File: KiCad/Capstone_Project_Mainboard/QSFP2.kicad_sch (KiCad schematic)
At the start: 12 parts, among them J4 QSFP+ Connector & Cage

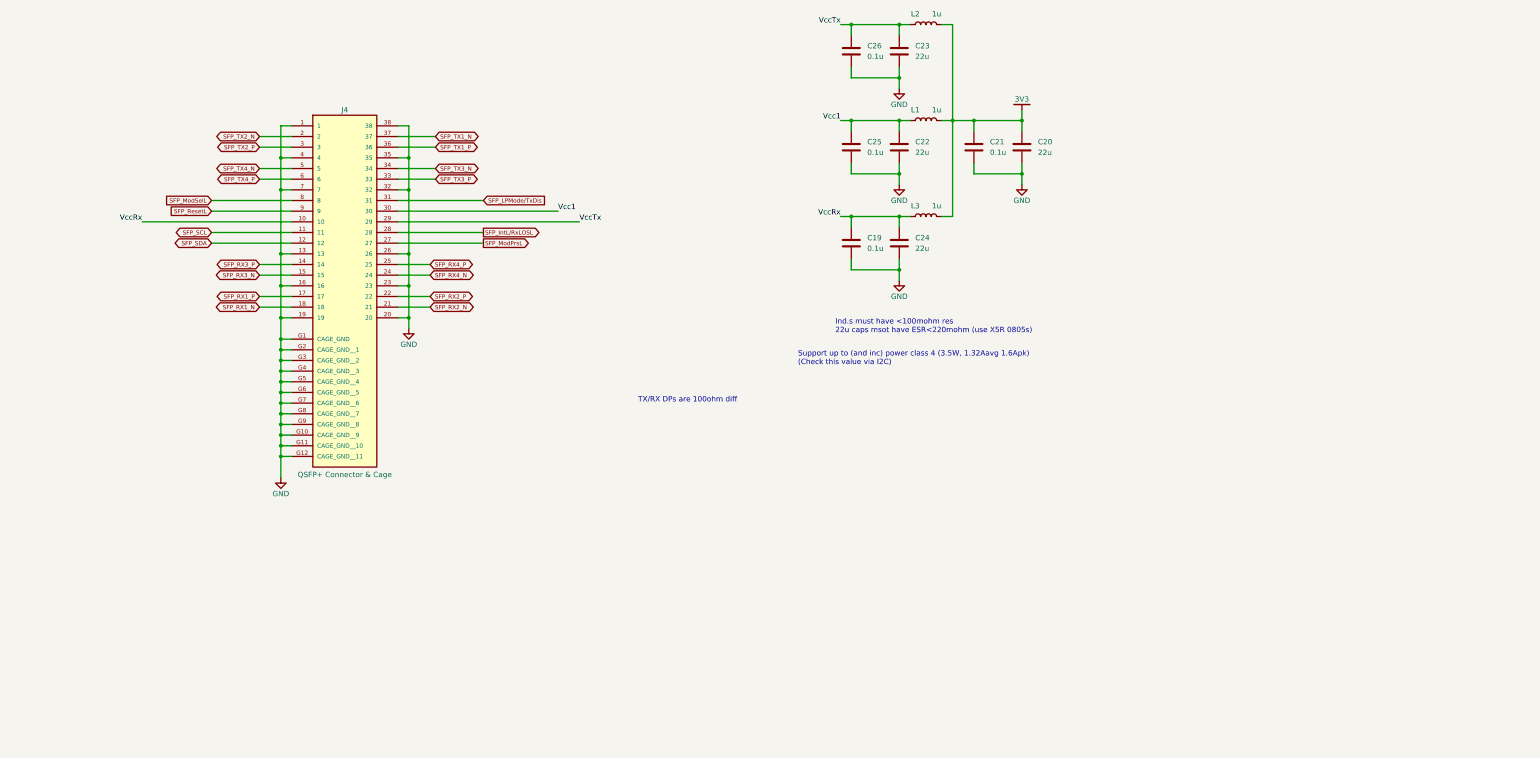
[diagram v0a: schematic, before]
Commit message: Core non-power parts defined
Most major non-power components added to KiCad project
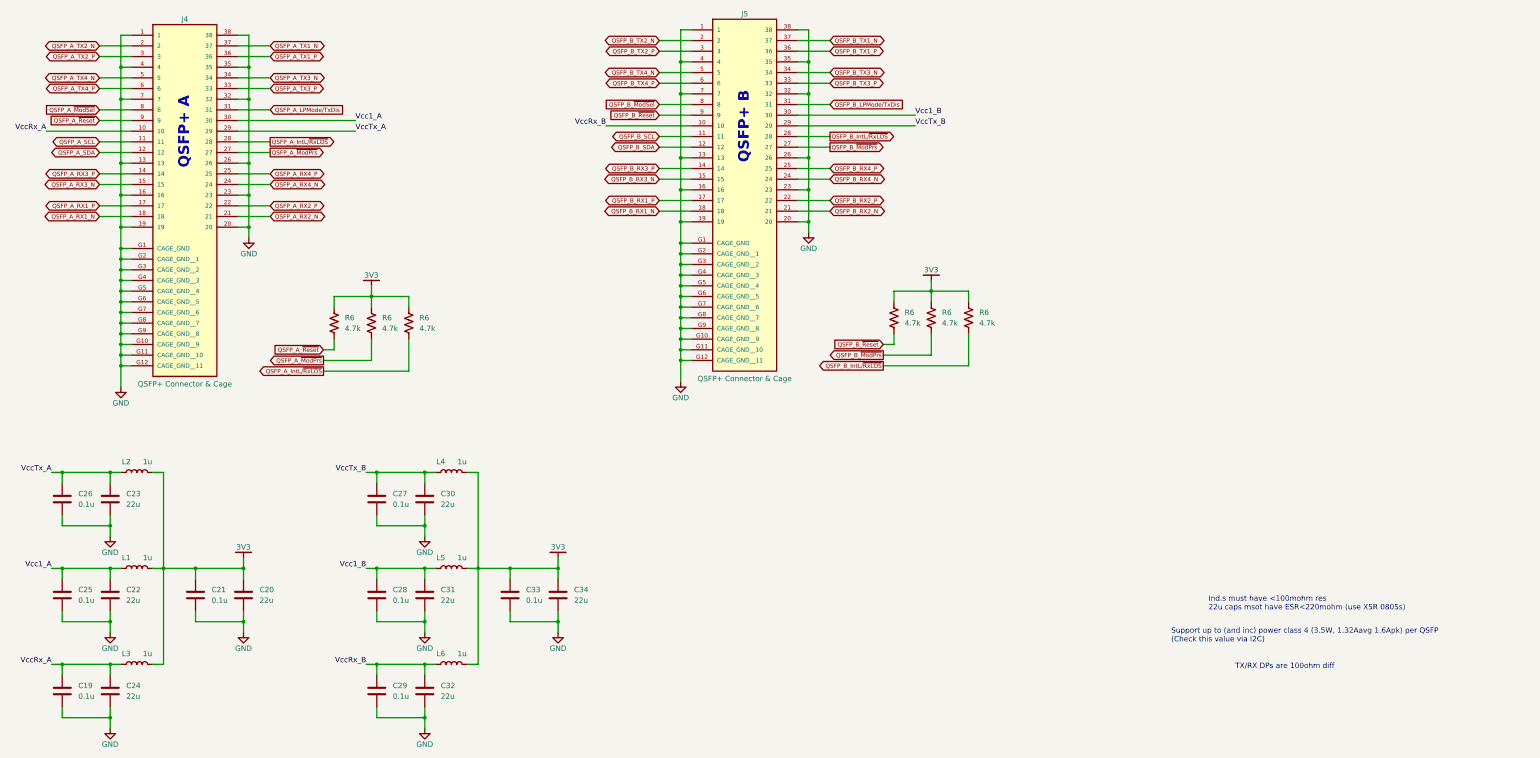
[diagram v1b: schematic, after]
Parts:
- added C27, C28, C29, C33: 0.1u, Capacitor_SMD:C_0402_1005Metric, symbol Device:C
- added C30, C31, C32, C34: 22u, Capacitor_SMD:C_0805_2012Metric, symbol Device:C
- added J5: QSFP+ Connector & Cage, Capstone_Library:AMPHENOL_U95T151100A, symbol Capstone_Library:U95T151100A+FS1Z3820Z660
- added L4, L5, L6: 1u, Inductor_SMD:L_1008_2520Metric, symbol Device:L
- added R6 (x6): 4.7k, Resistor_SMD:R_0402_1005Metric, symbol Device:R_US
- C19, C21, C25, C26: footprint (none) -> Capacitor_SMD:C_0402_1005Metric; Part Number (none) -> GRM155R71E104ME14J
- C20, C22, C23, C24: footprint (none) -> Capacitor_SMD:C_0805_2012Metric; Part Number (none) -> CL21A226MAYNNNE
- L1, L2, L3: footprint (none) -> Inductor_SMD:L_1008_2520Metric; Part Number (none) -> BDCD002520121R0MS1
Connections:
- net 3V3: now also C33.1, C34.1, L4.2, L5.2, L6.2, R6.1, R6.1, R6.1, R6.1, R6.1, R6.1
- net GND: now also C27.2, C28.2, C29.2, C30.2, C31.2, C32.2, C33.2, C34.2, J5.1, J5.13, J5.16, J5.19, J5.20, J5.23, J5.26, J5.32, J5.35, J5.38, J5.4, J5.7, J5.G1 (CAGE_GND), J5.G10 (CAGE_GND__9), J5.G11 (CAGE_GND__10), J5.G12 (CAGE_GND__11), J5.G2 (CAGE_GND__1), J5.G3 (CAGE_GND__2), J5.G4 (CAGE_GND__3), J5.G5 (CAGE_GND__4), J5.G6 (CAGE_GND__5), J5.G7 (CAGE_GND__6), J5.G8 (CAGE_GND__7), J5.G9 (CAGE_GND__8)
- net SFP_IntL/RxLOSL renamed QSFP_A_IntL/~{RxLOS}
- net QSFP_A_IntL/~{RxLOS}: now also R6.2
- net SFP_LPMode/TxDis renamed QSFP_A_LPMode/TxDis
- net SFP_ModPrsL renamed QSFP_A_~{ModPrs}
- net QSFP_A_~{ModPrs}: now also R6.2
- net SFP_ModSelL renamed QSFP_A_~{ModSel}
- net SFP_RX1_N renamed QSFP_A_RX1_N
- net SFP_RX1_P renamed QSFP_A_RX1_P
- net SFP_RX2_N renamed QSFP_A_RX2_N
- net SFP_RX2_P renamed QSFP_A_RX2_P
- net SFP_RX3_N renamed QSFP_A_RX3_N
- net SFP_RX3_P renamed QSFP_A_RX3_P
- net SFP_RX4_N renamed QSFP_A_RX4_N
- net SFP_RX4_P renamed QSFP_A_RX4_P
- net SFP_ResetL renamed QSFP_A_~{Reset}
- net QSFP_A_~{Reset}: now also R6.2
- net SFP_SCL renamed QSFP_A_SCL
- net SFP_SDA renamed QSFP_A_SDA
- net SFP_TX1_N renamed QSFP_A_TX1_N
- net SFP_TX1_P renamed QSFP_A_TX1_P
- net SFP_TX2_N renamed QSFP_A_TX2_N
- net SFP_TX2_P renamed QSFP_A_TX2_P
- net SFP_TX3_N renamed QSFP_A_TX3_N
- net SFP_TX3_P renamed QSFP_A_TX3_P
- net SFP_TX4_N renamed QSFP_A_TX4_N
- net SFP_TX4_P renamed QSFP_A_TX4_P
- net Vcc1 renamed Vcc1_A
- net VccRx renamed VccRx_A
- net VccTx renamed VccTx_A
- new net QSFP_B_IntL/~{RxLOS}: J5.28, R6.2
- new net QSFP_B_LPMode/TxDis: J5.31
- new net QSFP_B_RX1_N: J5.18
- new net QSFP_B_RX1_P: J5.17
- new net QSFP_B_RX2_N: J5.21
- new net QSFP_B_RX2_P: J5.22
- new net QSFP_B_RX3_N: J5.15
- new net QSFP_B_RX3_P: J5.14
- new net QSFP_B_RX4_N: J5.24
- new net QSFP_B_RX4_P: J5.25
- new net QSFP_B_SCL: J5.11
- new net QSFP_B_SDA: J5.12
- new net QSFP_B_TX1_N: J5.37
- new net QSFP_B_TX1_P: J5.36
- new net QSFP_B_TX2_N: J5.2
- new net QSFP_B_TX2_P: J5.3
- new net QSFP_B_TX3_N: J5.34
- new net QSFP_B_TX3_P: J5.33
- new net QSFP_B_TX4_N: J5.5
- new net QSFP_B_TX4_P: J5.6
- new net QSFP_B_~{ModPrs}: J5.27, R6.2
- new net QSFP_B_~{ModSel}: J5.8
- new net QSFP_B_~{Reset}: J5.9, R6.2
- new net Vcc1_B: C28.1, C31.1, J5.30, L5.1
- new net VccRx_B: C29.1, C32.1, J5.10, L6.1
- new net VccTx_B: C27.1, C30.1, J5.29, L4.1
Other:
- note added: "QSFP+ A"
- note added: "QSFP+ B"
- note added: "Support up to (and inc) power class 4 (3.5W, 1.32Aavg 1.6Apk) per QSFP (Check this value via I2C)"
- note removed: "Support up to (and inc) power class 4 (3.5W, 1.32Aavg 1.6Apk) (Check this value via I2C)"
- title: QSFP+ Connector -> QSFP+ Cages and Connectors
- moved on the sheet: C19, C20, C21, C22, C23, C24, C25, C26, J4, L1, L2, L3
